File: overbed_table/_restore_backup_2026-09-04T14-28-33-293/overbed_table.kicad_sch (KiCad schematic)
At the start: 0 parts

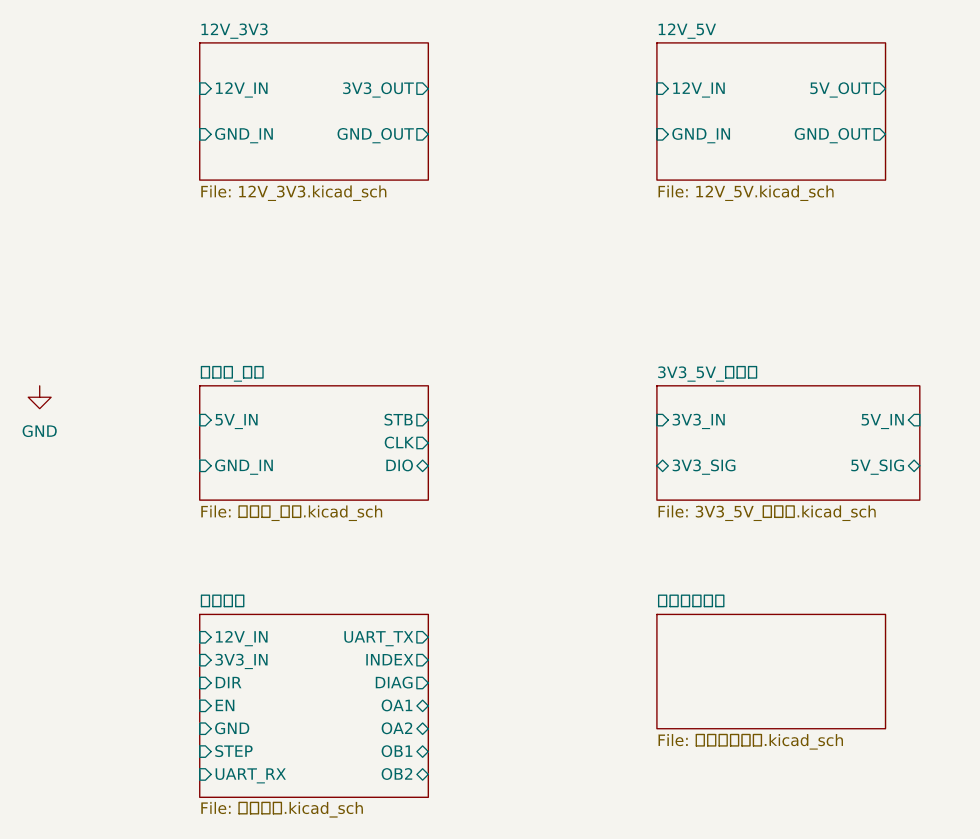
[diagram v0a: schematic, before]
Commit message: 更新步进驱动等
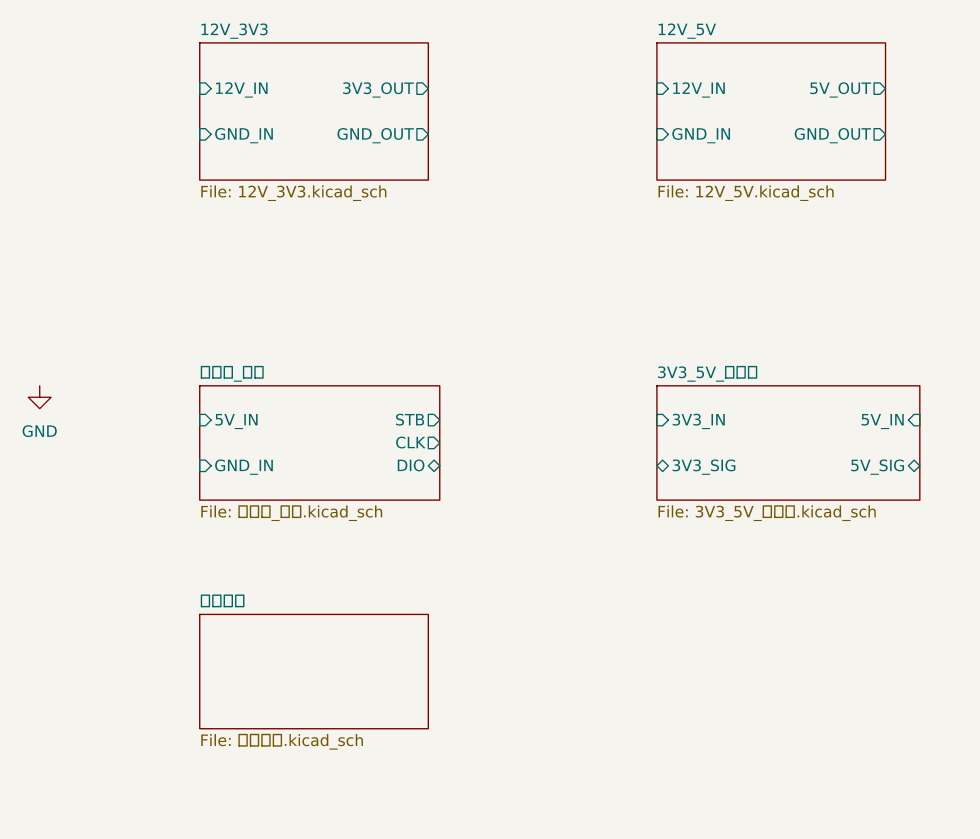
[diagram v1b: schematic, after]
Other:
- removed sheet 升降电机驱动
- sheet 步进驱动 ports: added none; removed 12V_IN, 3V3_IN, DIAG, DIR, EN, GND, INDEX, OA1, OA2, OB1, OB2, STEP, UART_RX, UART_TX
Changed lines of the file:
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@@
 	)
 	(sheet
-		(at 127 114.3)
+		(at 76.2 114.3)
 		(size 25.4 12.7)
 		(exclude_from_sim no)
@@
 		(dnp no)
 		(fields_autoplaced yes)
-		(stroke
-			(width 0.1524)
-			(type solid)
-		)
-		(fill
-			(color 0 0 0 0)
-		)
-		(property "Sheetname" "升降电机驱动"
-			(at 127 113.5884 0)
-			(show_name no)
-			(do_not_autoplace no)
-			(effects
-				(font
-					(size 1.27 1.27)
-				)
-				(justify left bottom)
-			)
-		)
-		(property "Sheetfile" "升降电机驱动.kicad_sch"
-			(at 127 127.5846 0)
-			(show_name no)
-			(do_not_autoplace no)
-			(effects
-				(font
-					(size 1.27 1.27)
-				)
-				(justify left top)
-			)
-		)
-		(instances
-			(project "overbed_table"
-				(path "/ea72387d-aa38-4027-b8fe-1f6fcfee6654"
-					(page "7")
-				)
-			)
-		)
-	)
-	(sheet
-		(at 76.2 114.3)
-		(size 25.4 20.32)
-		(exclude_from_sim no)
-		(in_bom yes)
-		(on_board yes)
-		(dnp no)
 		(stroke
 			(width 0.1524)
@@
 		)
 		(property "Sheetfile" "步进驱动.kicad_sch"
-			(at 76.2 135.128 0)
+			(at 76.2 127.5846 0)
 			(show_name no)
 			(do_not_autoplace no)
@@
 				)
 				(justify left top)
-			)
-		)
-		(pin "12V_IN" input
-			(at 76.2 116.84 180)
-			(effects
-				(font
-					(size 1.27 1.27)
-				)
-				(justify left)
-			)
-		)
-		(pin "3V3_IN" input
-			(at 76.2 119.38 180)
-			(effects
-				(font
-					(size 1.27 1.27)
-				)
-				(justify left)
-			)
-		)
-		(pin "DIR" input
-			(at 76.2 121.92 180)
-			(effects
-				(font
-					(size 1.27 1.27)
-				)
-				(justify left)
-			)
-		)
-		(pin "EN" input
-			(at 76.2 124.46 180)
-			(effects
-				(font
-					(size 1.27 1.27)
-				)
-				(justify left)
-			)
-		)
-		(pin "GND" input
-			(at 76.2 127 180)
-			(effects
-				(font
-					(size 1.27 1.27)
-				)
-				(justify left)
-			)
-		)
-		(pin "OA1" bidirectional
-			(at 101.6 124.46 0)
-			(effects
-				(font
-					(size 1.27 1.27)
-				)
-				(justify right)
-			)
-		)
-		(pin "OA2" bidirectional
-			(at 101.6 127 0)
-			(effects
-				(font
-					(size 1.27 1.27)
-				)
-				(justify right)
-			)
-		)
-		(pin "OB1" bidirectional
-			(at 101.6 129.54 0)
-			(effects
-				(font
-					(size 1.27 1.27)
-				)
-				(justify right)
-			)
-		)
-		(pin "OB2" bidirectional
-			(at 101.6 132.08 0)
-			(effects
-				(font
-					(size 1.27 1.27)
-				)
-				(justify right)
-			)
-		)
-		(pin "STEP" input
-			(at 76.2 129.54 180)
-			(effects
-				(font
-					(size 1.27 1.27)
-				)
-				(justify left)
-			)
-		)
-		(pin "UART_RX" input
-			(at 76.2 132.08 180)
-			(effects
-				(font
-					(size 1.27 1.27)
-				)
-				(justify left)
-			)
-		)
-		(pin "DIAG" output
-			(at 101.6 121.92 0)
-			(effects
-				(font
-					(size 1.27 1.27)
-				)
-				(justify right)
-			)
-		)
-		(pin "INDEX" output
-			(at 101.6 119.38 0)
-			(effects
-				(font
-					(size 1.27 1.27)
-				)
-				(justify right)
-			)
-		)
-		(pin "UART_TX" output
-			(at 101.6 116.84 0)
-			(effects
-				(font
-					(size 1.27 1.27)
-				)
-				(justify right)
 			)
 		)
@@
 	(sheet
 		(at 76.2 88.9)
-		(size 25.4 12.7)
+		(size 26.67 12.7)
 		(exclude_from_sim no)
 		(in_bom yes)
@@
 		)
 		(pin "CLK" output
-			(at 101.6 95.25 0)
+			(at 102.87 95.25 0)
 			(effects
 				(font
@@
 		)
 		(pin "DIO" bidirectional
-			(at 101.6 97.79 0)
+			(at 102.87 97.79 0)
 			(effects
 				(font
@@
 		)
 		(pin "STB" output
-			(at 101.6 92.71 0)
+			(at 102.87 92.71 0)
 			(effects
 				(font
